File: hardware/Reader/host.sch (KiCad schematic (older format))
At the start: 5 parts

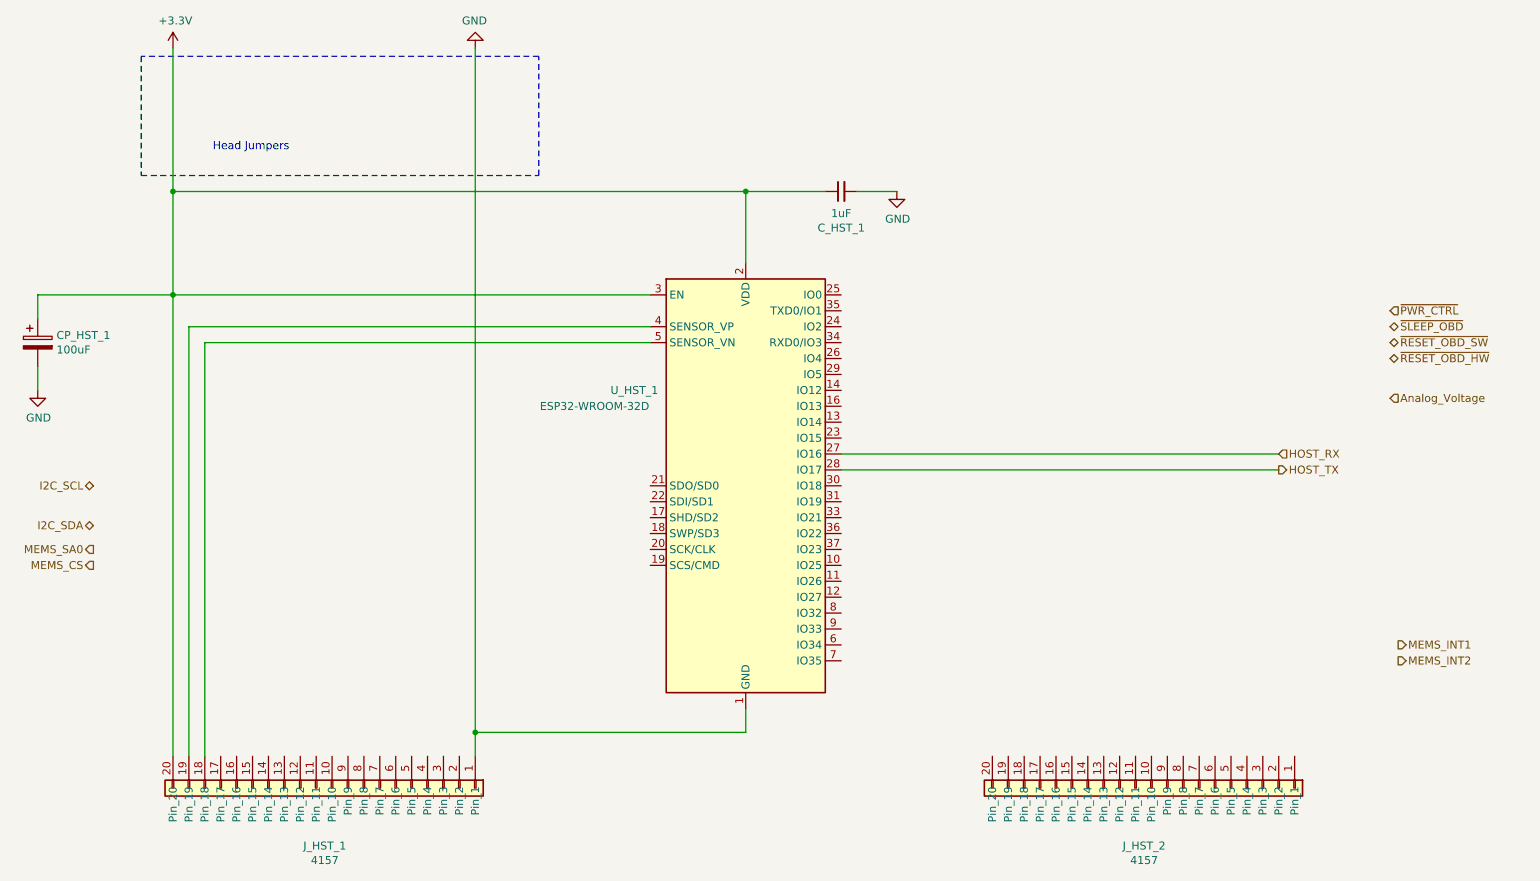
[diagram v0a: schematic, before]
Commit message: Updated reader schematic to v0.0.5 by adding ESP32, removing unused transceivers, fixed design flaws, increased header pins and fixed footprints. Working on reader PCB design
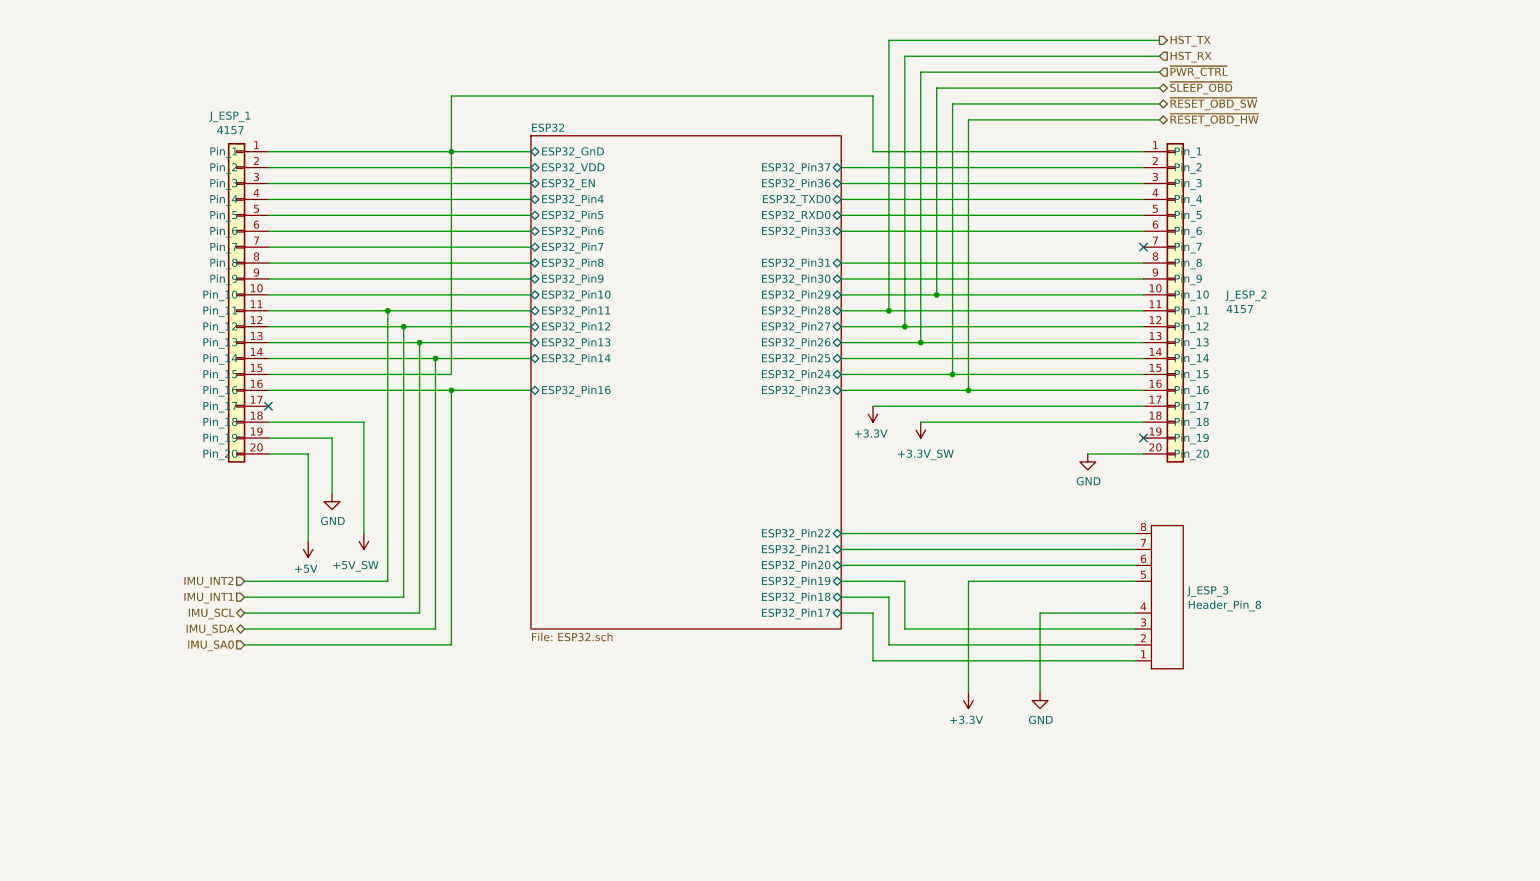
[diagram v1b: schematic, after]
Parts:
- removed CP_HST_1: 100uF, footprints:UCB0J101MCL1GS, symbol Device:CP
- removed C_HST_1: 1uF, footprints:0603, symbol Device:C_Small
- removed J_HST_1, J_HST_2: 4157, Connector_PinSocket_2.54mm:PinSocket_1x20_P2.54mm_Vertical, symbol CANtech:4157
- removed U_HST_1: ESP32-WROOM-32D, RF_Module:ESP32-WROOM-32, symbol RF_Module:ESP32-WROOM-32D
- added J_ESP_1, J_ESP_2: 4157, Connector_PinSocket_2.54mm:PinSocket_1x20_P2.54mm_Vertical, symbol CANtech:4157
- added J_ESP_3: Header_Pin_8, Connector_PinHeader_2.54mm:PinHeader_1x08_P2.54mm_Vertical, symbol CANtech:Header_Pin_8
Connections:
- net +3V3: now also J_ESP_2.17 (Pin_17), J_ESP_3.5
- net GND: now also J_ESP_1.19 (Pin_19), J_ESP_2.20 (Pin_20), J_ESP_3.4
- net ~PWR_CTRL~: now also J_ESP_2.13 (Pin_13)
- net ~RESET_OBD_HW~: now also J_ESP_2.16 (Pin_16)
- net ~RESET_OBD_SW~: now also J_ESP_2.15 (Pin_15)
- net ~SLEEP_OBD~: now also J_ESP_2.10 (Pin_10)
- new net +3.3V_SW: J_ESP_2.18 (Pin_18)
- new net +5V: J_ESP_1.20 (Pin_20)
- new net +5V_SW: J_ESP_1.18 (Pin_18)
- new net ESP32/ESP32_EN: J_ESP_1.3 (Pin_3)
- new net ESP32/ESP32_GnD: J_ESP_1.1 (Pin_1), J_ESP_1.15 (Pin_15), J_ESP_2.1 (Pin_1)
- new net ESP32/ESP32_Pin10: J_ESP_1.10 (Pin_10)
- new net ESP32/ESP32_Pin17: J_ESP_3.1
- new net ESP32/ESP32_Pin18: J_ESP_3.2
- new net ESP32/ESP32_Pin19: J_ESP_3.3
- new net ESP32/ESP32_Pin20: J_ESP_3.6
- new net ESP32/ESP32_Pin21: J_ESP_3.7
- new net ESP32/ESP32_Pin22: J_ESP_3.8
- new net ESP32/ESP32_Pin25: J_ESP_2.14 (Pin_14)
- new net ESP32/ESP32_Pin30: J_ESP_2.9 (Pin_9)
- new net ESP32/ESP32_Pin31: J_ESP_2.8 (Pin_8)
- new net ESP32/ESP32_Pin33: J_ESP_2.6 (Pin_6)
- new net ESP32/ESP32_Pin36: J_ESP_2.3 (Pin_3)
- new net ESP32/ESP32_Pin37: J_ESP_2.2 (Pin_2)
- new net ESP32/ESP32_Pin4: J_ESP_1.4 (Pin_4)
- new net ESP32/ESP32_Pin5: J_ESP_1.5 (Pin_5)
- new net ESP32/ESP32_Pin6: J_ESP_1.6 (Pin_6)
- new net ESP32/ESP32_Pin7: J_ESP_1.7 (Pin_7)
- new net ESP32/ESP32_Pin8: J_ESP_1.8 (Pin_8)
- new net ESP32/ESP32_Pin9: J_ESP_1.9 (Pin_9)
- new net ESP32/ESP32_RXD0: J_ESP_2.5 (Pin_5)
- new net ESP32/ESP32_TXD0: J_ESP_2.4 (Pin_4)
- new net ESP32/ESP32_VDD: J_ESP_1.2 (Pin_2)
- new net HST_RX: J_ESP_2.12 (Pin_12)
- new net HST_TX: J_ESP_2.11 (Pin_11)
- new net IMU_INT1: J_ESP_1.12 (Pin_12)
- new net IMU_INT2: J_ESP_1.11 (Pin_11)
- new net IMU_SA0: J_ESP_1.16 (Pin_16)
- new net IMU_SCL: J_ESP_1.13 (Pin_13)
- new net IMU_SDA: J_ESP_1.14 (Pin_14)
- no-connect marks 0 -> 3
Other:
- note removed: "Head Jumpers"

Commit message: Updated schematic and gerber to v0.0.05. Added ESP32. Removed MS CAN and SW CAN Transceivers. Added silkscreen text to header pins. Improved readability
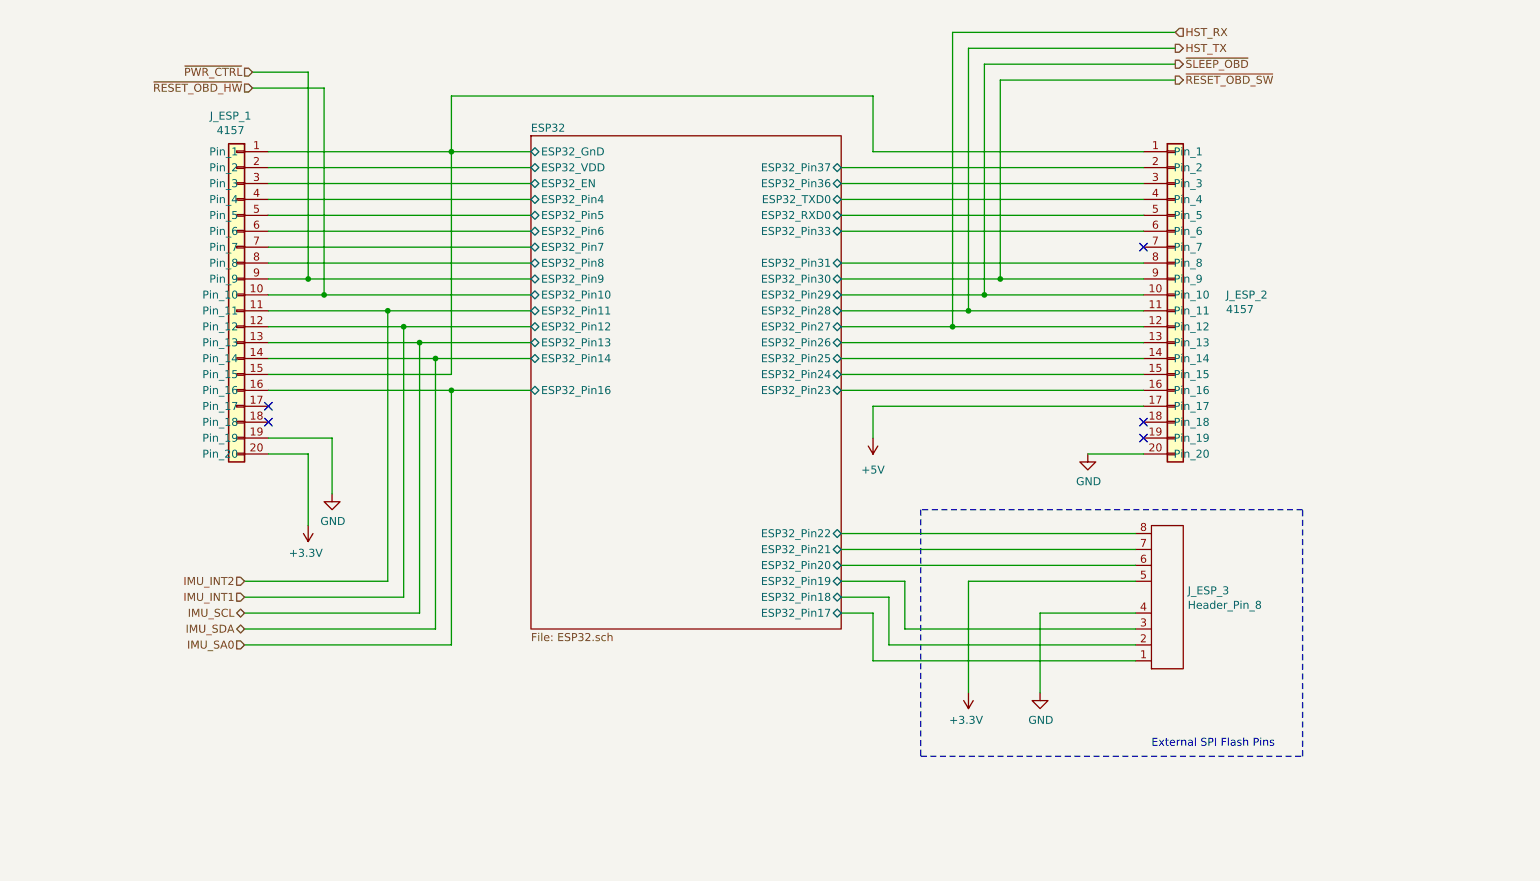
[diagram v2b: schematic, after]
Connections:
- net ESP32/ESP32_Pin10 is gone; now on net ~RESET_OBD_HW~: J_ESP_1.10 (Pin_10)
- net ESP32/ESP32_Pin30 is gone; now on net ~RESET_OBD_SW~: J_ESP_2.9 (Pin_9)
- net ESP32/ESP32_Pin9 is gone; now on net ~PWR_CTRL~: J_ESP_1.9 (Pin_9)
- net +3V3: now also J_ESP_1.20 (Pin_20); no longer J_ESP_2.17 (Pin_17)
- net +5V: now also J_ESP_2.17 (Pin_17); no longer J_ESP_1.20 (Pin_20)
- net ~PWR_CTRL~: no longer J_ESP_2.13 (Pin_13)
- net ~RESET_OBD_HW~: no longer J_ESP_2.16 (Pin_16)
- net ~RESET_OBD_SW~: no longer J_ESP_2.15 (Pin_15)
- net +3.3V_SW: no longer names the net of J_ESP_2.18 (Pin_18)
- net +5V_SW: no longer names the net of J_ESP_1.18 (Pin_18)
- new net ESP32/ESP32_Pin23: J_ESP_2.16 (Pin_16)
- new net ESP32/ESP32_Pin24: J_ESP_2.15 (Pin_15)
- new net ESP32/ESP32_Pin26: J_ESP_2.13 (Pin_13)
- no-connect marks 3 -> 5
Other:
- note added: "External SPI Flash Pins"
